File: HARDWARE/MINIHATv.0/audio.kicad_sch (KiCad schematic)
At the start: 1 part, among them U4 TAD5142

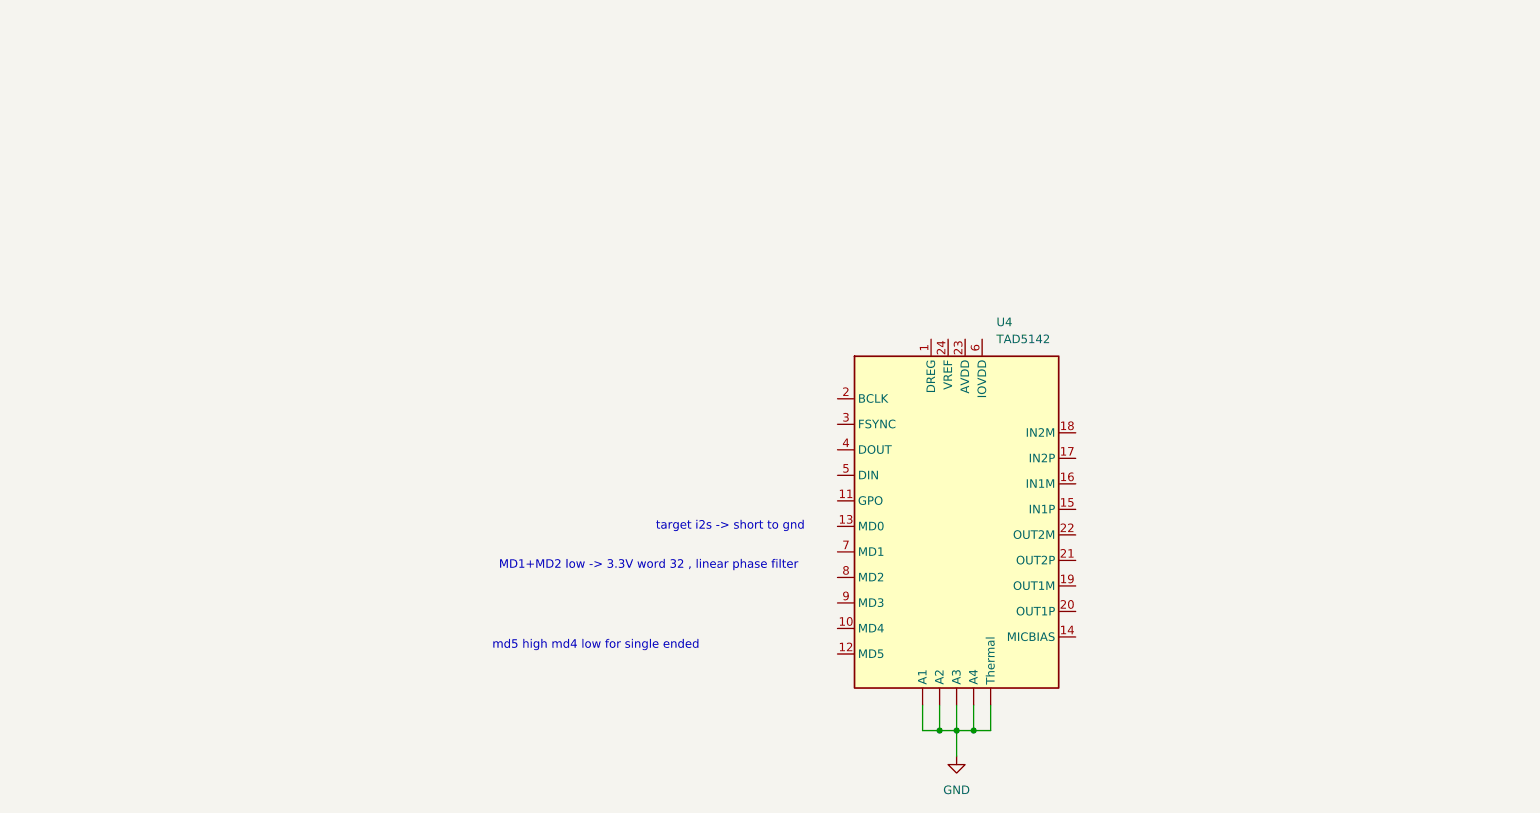
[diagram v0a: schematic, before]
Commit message: added digital part of audio schematic
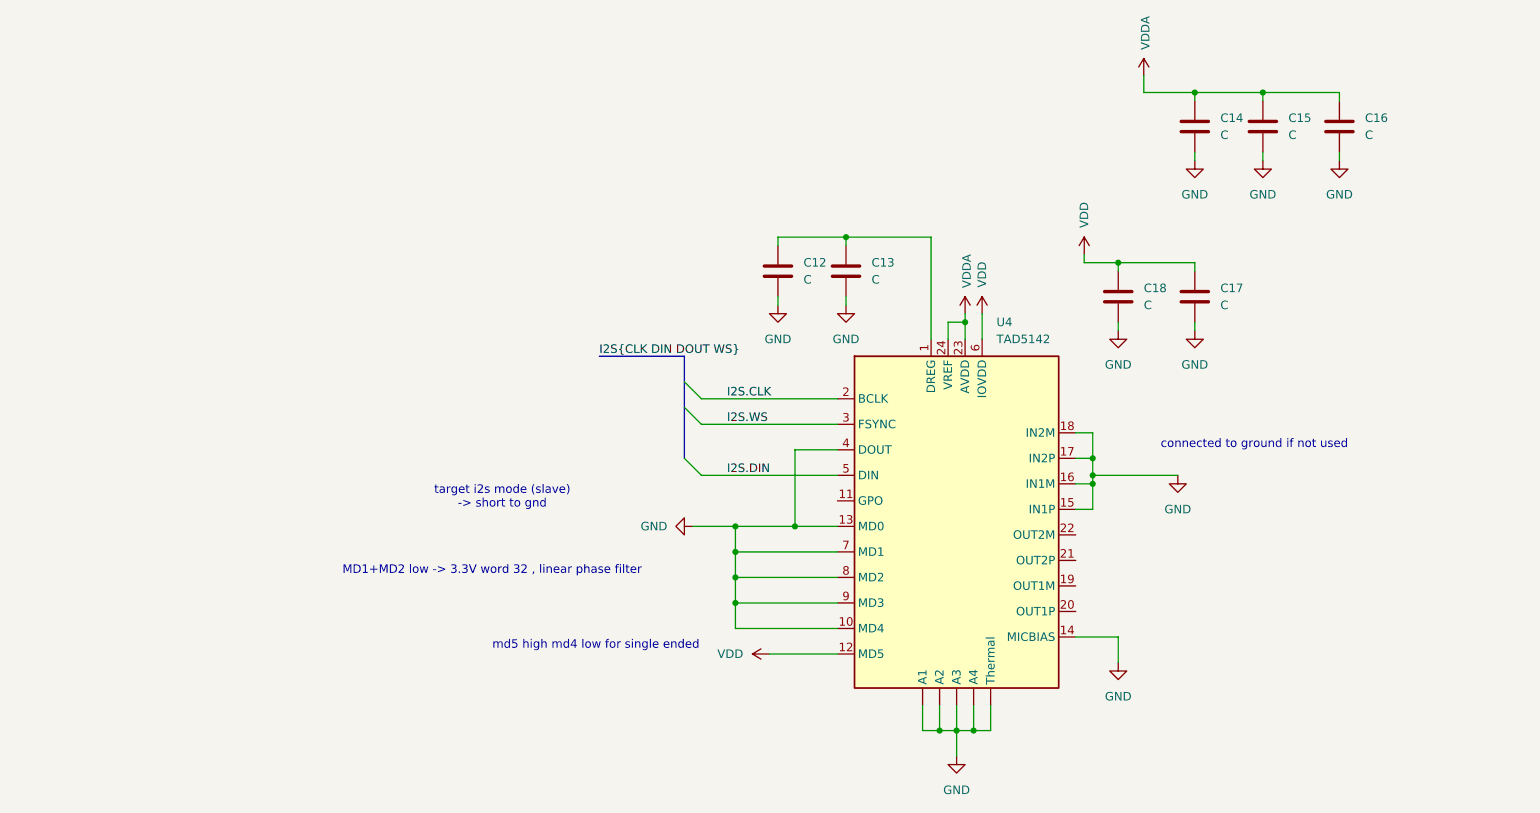
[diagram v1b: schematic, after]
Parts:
- added C12, C13, C14, C15, C16, C17, C18: C, symbol Device:C
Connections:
- net GND: now also U4.10 (MD4), U4.13 (MD0), U4.14 (MICBIAS), U4.15 (IN1P), U4.16 (IN1M), U4.17 (IN2P), U4.18 (IN2M), U4.4 (DOUT), U4.7 (MD1), U4.8 (MD2), U4.9 (MD3), C12.2, C13.2, C14.2, C15.2, C16.2, C17.2, C18.2
- net at U4.1 (DREG): now also C12.1, C13.1
- net VDD: now reaches U4.12 (MD5)
- net VDD: now also U4.6 (IOVDD), C17.1, C18.1
- net I2S.CLK: now reaches U4.2 (BCLK)
- net VDDA: now reaches U4.23 (AVDD)
- net VDDA: now also U4.24 (VREF), C14.1, C15.1, C16.1
- net I2S.WS: now reaches U4.3 (FSYNC)
- net I2S.DIN: now reaches U4.5 (DIN)
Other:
- note added: "connected to ground if not used"
- note added: "target i2s mode (slave) -> short to gnd"
- note removed: "target i2s -> short to gnd"

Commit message: updated audio ic and schematic
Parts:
- added J3: AudioJack3, symbol Connector_Audio:AudioJack3
- added R40, R41: R, symbol Device:R
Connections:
- net at U4.19 (OUT1M): now also U4.22 (OUT2M), J3.S, R40.2, R41.1
- net at U4.20 (OUT1P): now also J3.T, R41.2
- net at U4.21 (OUT2P): now also J3.R, R40.1
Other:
- note removed: "connected to ground if not used"
- moved on the sheet: U4

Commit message: audio page added to top
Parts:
- renumbered C12 to C90, C13 to C91, C18 to C92, C14 to C93, C17 to C94, C15 to C95, C16 to C96, J3 to J8, R40 to R89, R41 to R90, U4 to U12
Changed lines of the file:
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@@
 	(bus
 		(pts
-			(xy 33.02 29.21) (xy 45.72 29.21)
+			(xy 40.64 29.21) (xy 45.72 29.21)
 		)
 		(stroke
@@
 		)
 	)
-	(label "I2S{CLK DIN DOUT WS}"
-		(at 33.02 29.21 0)
-		(effects
-			(font
-				(size 1.27 1.27)
-			)
-			(justify left bottom)
-		)
-	)
 	(label "I2S.CLK"
 		(at 58.42 35.56 180)
@@
 		)
 	)
-	(label "I2S{CLK DIN DOUT WS}"
-		(at 100.33 71.12 0)
-		(effects
-			(font
-				(size 1.27 1.27)
-			)
-			(justify left bottom)
-		)
-	)
 	(label "I2S.DIN"
 		(at 58.42 40.64 180)
@@
 			)
 			(justify left bottom)
+		)
+	)
+	(hierarchical_label "I2S{CLK DIN DOUT WS}"
+		(shape input)
+		(at 100.33 71.12 180)
+		(effects
+			(font
+				(size 1.27 1.27)
+			)
+			(justify right)
+		)
+	)
+	(hierarchical_label "I2S{CLK DIN DOUT WS}"
+		(shape input)
+		(at 40.64 29.21 180)
+		(effects
+			(font
+				(size 1.27 1.27)
+			)
+			(justify right)
 		)
 	)
@@
 		(dnp no)
 		(fields_autoplaced yes)
-		(property "Reference" "R41"
+		(property "Reference" "R90"
 			(at 190.5 100.3299 0)
 			(show_name no)
@@
 		(instances
 			(project "MINIHATv.0"
-				(path "/19041ef4-1d16-4363-8780-721ad9f20b33/d3a2965b-be57-4039-bff6-a76ba7e31272"
-					(reference "R41")
+				(path "/19041ef4-1d16-4363-8780-721ad9f20b33/cfc8326a-d42a-4b01-8fc0-0e46d075417e"
+					(reference "R90")
 					(unit 1)
 				)
@@
 		(instances
 			(project "MINIHATv.0"
-				(path "/19041ef4-1d16-4363-8780-721ad9f20b33/d3a2965b-be57-4039-bff6-a76ba7e31272"
+				(path "/19041ef4-1d16-4363-8780-721ad9f20b33/cfc8326a-d42a-4b01-8fc0-0e46d075417e"
 					(reference "#PWR042")
 					(unit 1)
@@
 		(instances
 			(project "MINIHATv.0"
-				(path "/19041ef4-1d16-4363-8780-721ad9f20b33/d3a2965b-be57-4039-bff6-a76ba7e31272"
+				(path "/19041ef4-1d16-4363-8780-721ad9f20b33/cfc8326a-d42a-4b01-8fc0-0e46d075417e"
 					(reference "#PWR032")
 					(unit 1)
@@
 		(dnp no)
 		(fields_autoplaced yes)
-		(property "Reference" "C15"
+		(property "Reference" "C95"
 			(at 203.2 35.5599 0)
 			(show_name no)
@@
 		(instances
 			(project "MINIHATv.0"
-				(path "/19041ef4-1d16-4363-8780-721ad9f20b33/d3a2965b-be57-4039-bff6-a76ba7e31272"
-					(reference "C15")
+				(path "/19041ef4-1d16-4363-8780-721ad9f20b33/cfc8326a-d42a-4b01-8fc0-0e46d075417e"
+					(reference "C95")
 					(unit 1)
 				)
@@
 		(dnp no)
 		(fields_autoplaced yes)
-		(property "Reference" "R40"
+		(property "Reference" "R89"
 			(at 190.5 81.2799 0)
 			(show_name no)
@@
 		(instances
 			(project "MINIHATv.0"
-				(path "/19041ef4-1d16-4363-8780-721ad9f20b33/d3a2965b-be57-4039-bff6-a76ba7e31272"
-					(reference "R40")
+				(path "/19041ef4-1d16-4363-8780-721ad9f20b33/cfc8326a-d42a-4b01-8fc0-0e46d075417e"
+					(reference "R89")
 					(unit 1)
 				)
@@
 		(instances
 			(project "MINIHATv.0"
-				(path "/19041ef4-1d16-4363-8780-721ad9f20b33/d3a2965b-be57-4039-bff6-a76ba7e31272"
+				(path "/19041ef4-1d16-4363-8780-721ad9f20b33/cfc8326a-d42a-4b01-8fc0-0e46d075417e"
 					(reference "#PWR043")
 					(unit 1)
@@
 		(instances
 			(project "MINIHATv.0"
-				(path "/19041ef4-1d16-4363-8780-721ad9f20b33/d3a2965b-be57-4039-bff6-a76ba7e31272"
+				(path "/19041ef4-1d16-4363-8780-721ad9f20b33/cfc8326a-d42a-4b01-8fc0-0e46d075417e"
 					(reference "#PWR037")
 					(unit 1)
@@
 		(instances
 			(project "MINIHATv.0"
-				(path "/19041ef4-1d16-4363-8780-721ad9f20b33/d3a2965b-be57-4039-bff6-a76ba7e31272"
+				(path "/19041ef4-1d16-4363-8780-721ad9f20b33/cfc8326a-d42a-4b01-8fc0-0e46d075417e"
 					(reference "#PWR036")
 					(unit 1)
@@
 		(instances
 			(project "MINIHATv.0"
-				(path "/19041ef4-1d16-4363-8780-721ad9f20b33/d3a2965b-be57-4039-bff6-a76ba7e31272"
+				(path "/19041ef4-1d16-4363-8780-721ad9f20b33/cfc8326a-d42a-4b01-8fc0-0e46d075417e"
 					(reference "#PWR039")
 					(unit 1)
@@
 		(instances
 			(project "MINIHATv.0"
-				(path "/19041ef4-1d16-4363-8780-721ad9f20b33/d3a2965b-be57-4039-bff6-a76ba7e31272"
+				(path "/19041ef4-1d16-4363-8780-721ad9f20b33/cfc8326a-d42a-4b01-8fc0-0e46d075417e"
 					(reference "#PWR040")
 					(unit 1)
@@
 		(dnp no)
 		(fields_autoplaced yes)
-		(property "Reference" "C12"
+		(property "Reference" "C90"
 			(at 130.81 57.1499 0)
 			(show_name no)
@@
 		(instances
 			(project "MINIHATv.0"
-				(path "/19041ef4-1d16-4363-8780-721ad9f20b33/d3a2965b-be57-4039-bff6-a76ba7e31272"
-					(reference "C12")
+				(path "/19041ef4-1d16-4363-8780-721ad9f20b33/cfc8326a-d42a-4b01-8fc0-0e46d075417e"
+					(reference "C90")
 					(unit 1)
 				)
@@
 		(instances
 			(project "MINIHATv.0"
-				(path "/19041ef4-1d16-4363-8780-721ad9f20b33/d3a2965b-be57-4039-bff6-a76ba7e31272"
+				(path "/19041ef4-1d16-4363-8780-721ad9f20b33/cfc8326a-d42a-4b01-8fc0-0e46d075417e"
 					(reference "#PWR044")
 					(unit 1)
@@
 		(instances
 			(project "MINIHATv.0"
-				(path "/19041ef4-1d16-4363-8780-721ad9f20b33/d3a2965b-be57-4039-bff6-a76ba7e31272"
+				(path "/19041ef4-1d16-4363-8780-721ad9f20b33/cfc8326a-d42a-4b01-8fc0-0e46d075417e"
 					(reference "#PWR047")
 					(unit 1)
@@
 		(dnp no)
 		(fields_autoplaced yes)
-		(property "Reference" "U4"
+		(property "Reference" "U12"
 			(at 167.894 66.548 0)
 			(show_name no)
@@
 		(instances
 			(project "MINIHATv.0"
-				(path "/19041ef4-1d16-4363-8780-721ad9f20b33/d3a2965b-be57-4039-bff6-a76ba7e31272"
-					(reference "U4")
+				(path "/19041ef4-1d16-4363-8780-721ad9f20b33/cfc8326a-d42a-4b01-8fc0-0e46d075417e"
+					(reference "U12")
 					(unit 1)
 				)
@@
 		(dnp no)
 		(fields_autoplaced yes)
-		(property "Reference" "C14"
+		(property "Reference" "C93"
 			(at 193.04 35.5599 0)
 			(show_name no)
@@
 		(instances
 			(project "MINIHATv.0"
-				(path "/19041ef4-1d16-4363-8780-721ad9f20b33/d3a2965b-be57-4039-bff6-a76ba7e31272"
-					(reference "C14")
+				(path "/19041ef4-1d16-4363-8780-721ad9f20b33/cfc8326a-d42a-4b01-8fc0-0e46d075417e"
+					(reference "C93")
 					(unit 1)
 				)
@@
 		(instances
 			(project "MINIHATv.0"
-				(path "/19041ef4-1d16-4363-8780-721ad9f20b33/d3a2965b-be57-4039-bff6-a76ba7e31272"
+				(path "/19041ef4-1d16-4363-8780-721ad9f20b33/cfc8326a-d42a-4b01-8fc0-0e46d075417e"
 					(reference "#PWR035")
 					(unit 1)
@@
 		(instances
 			(project "MINIHATv.0"
-				(path "/19041ef4-1d16-4363-8780-721ad9f20b33/d3a2965b-be57-4039-bff6-a76ba7e31272"
+				(path "/19041ef4-1d16-4363-8780-721ad9f20b33/cfc8326a-d42a-4b01-8fc0-0e46d075417e"
 					(reference "#PWR041")
 					(unit 1)
@@
 		(instances
 			(project "MINIHATv.0"
-				(path "/19041ef4-1d16-4363-8780-721ad9f20b33/d3a2965b-be57-4039-bff6-a76ba7e31272"
+				(path "/19041ef4-1d16-4363-8780-721ad9f20b33/cfc8326a-d42a-4b01-8fc0-0e46d075417e"
 					(reference "#PWR034")
 					(unit 1)
@@
 		(dnp no)
 		(fields_autoplaced yes)
-		(property "Reference" "C13"
+		(property "Reference" "C91"
 			(at 140.97 57.1499 0)
 			(show_name no)
@@
 		(instances
 			(project "MINIHATv.0"
-				(path "/19041ef4-1d16-4363-8780-721ad9f20b33/d3a2965b-be57-4039-bff6-a76ba7e31272"
-					(reference "C13")
+				(path "/19041ef4-1d16-4363-8780-721ad9f20b33/cfc8326a-d42a-4b01-8fc0-0e46d075417e"
+					(reference "C91")
 					(unit 1)
 				)
@@
 		(in_pos_files yes)
 		(dnp no)
-		(property "Reference" "J3"
+		(property "Reference" "J8"
 			(at 226.06 90.8049 0)
 			(show_name no)
@@
 		(instances
 			(project "MINIHATv.0"
-				(path "/19041ef4-1d16-4363-8780-721ad9f20b33/d3a2965b-be57-4039-bff6-a76ba7e31272"
-					(reference "J3")
+				(path "/19041ef4-1d16-4363-8780-721ad9f20b33/cfc8326a-d42a-4b01-8fc0-0e46d075417e"
+					(reference "J8")
 					(unit 1)
 				)
@@
 		(dnp no)
 		(fields_autoplaced yes)
-		(property "Reference" "C17"
+		(property "Reference" "C94"
 			(at 193.04 60.9599 0)
 			(show_name no)
@@
 		(instances
 			(project "MINIHATv.0"
-				(path "/19041ef4-1d16-4363-8780-721ad9f20b33/d3a2965b-be57-4039-bff6-a76ba7e31272"
-					(reference "C17")
+				(path "/19041ef4-1d16-4363-8780-721ad9f20b33/cfc8326a-d42a-4b01-8fc0-0e46d075417e"
+					(reference "C94")
 					(unit 1)
 				)
@@
 		(dnp no)
 		(fields_autoplaced yes)
-		(property "Reference" "C18"
+		(property "Reference" "C92"
 			(at 181.61 60.9599 0)
 			(show_name no)
@@
 		(instances
 			(project "MINIHATv.0"
-				(path "/19041ef4-1d16-4363-8780-721ad9f20b33/d3a2965b-be57-4039-bff6-a76ba7e31272"
-					(reference "C18")
+				(path "/19041ef4-1d16-4363-8780-721ad9f20b33/cfc8326a-d42a-4b01-8fc0-0e46d075417e"
+					(reference "C92")
 					(unit 1)
 				)
@@
 		(dnp no)
 		(fields_autoplaced yes)
-		(property "Reference" "C16"
+		(property "Reference" "C96"
 			(at 214.63 35.5599 0)
 			(show_name no)
@@
 		(instances
 			(project "MINIHATv.0"
-				(path "/19041ef4-1d16-4363-8780-721ad9f20b33/d3a2965b-be57-4039-bff6-a76ba7e31272"
-					(reference "C16")
+				(path "/19041ef4-1d16-4363-8780-721ad9f20b33/cfc8326a-d42a-4b01-8fc0-0e46d075417e"
+					(reference "C96")
 					(unit 1)
 				)
@@
 		(instances
 			(project "MINIHATv.0"
-				(path "/19041ef4-1d16-4363-8780-721ad9f20b33/d3a2965b-be57-4039-bff6-a76ba7e31272"
+				(path "/19041ef4-1d16-4363-8780-721ad9f20b33/cfc8326a-d42a-4b01-8fc0-0e46d075417e"
 					(reference "#PWR038")
 					(unit 1)
